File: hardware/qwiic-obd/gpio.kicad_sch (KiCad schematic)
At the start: 25 parts, among them J401 1x4, SW401 SW_Push, SW402 SW_Push, U401 TCA9534, U402 MCP3423, U403 TCA9534, U404 APX823-31W5G-7

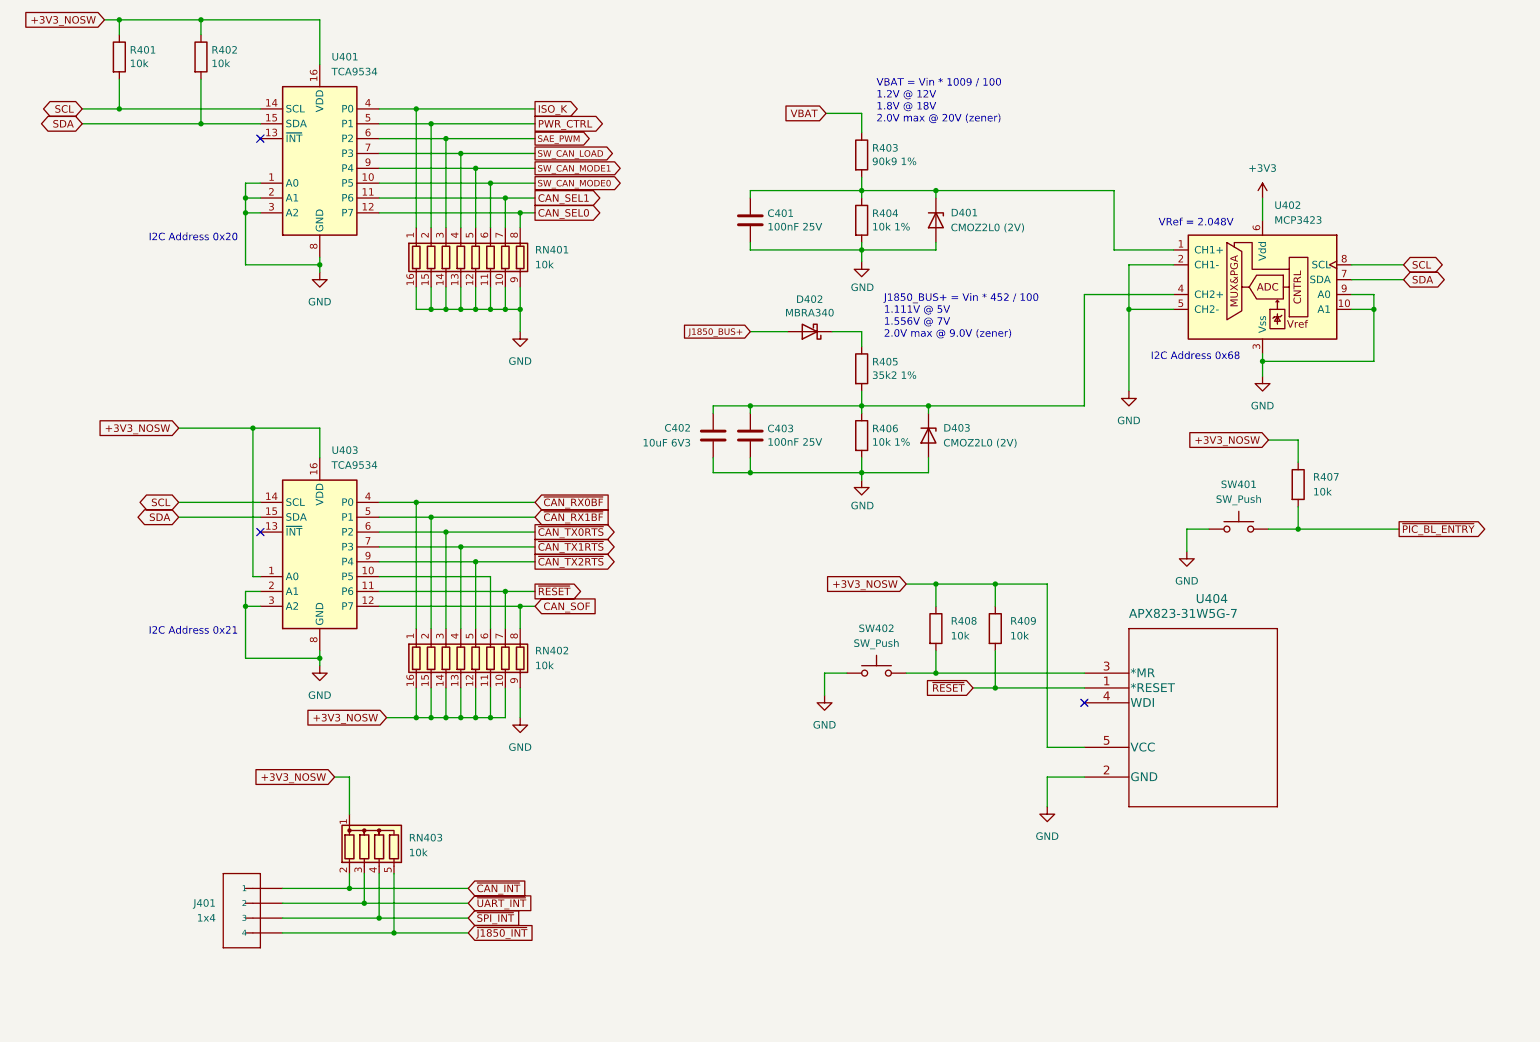
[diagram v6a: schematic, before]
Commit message: Switch out the PIC for an ATtiny424.
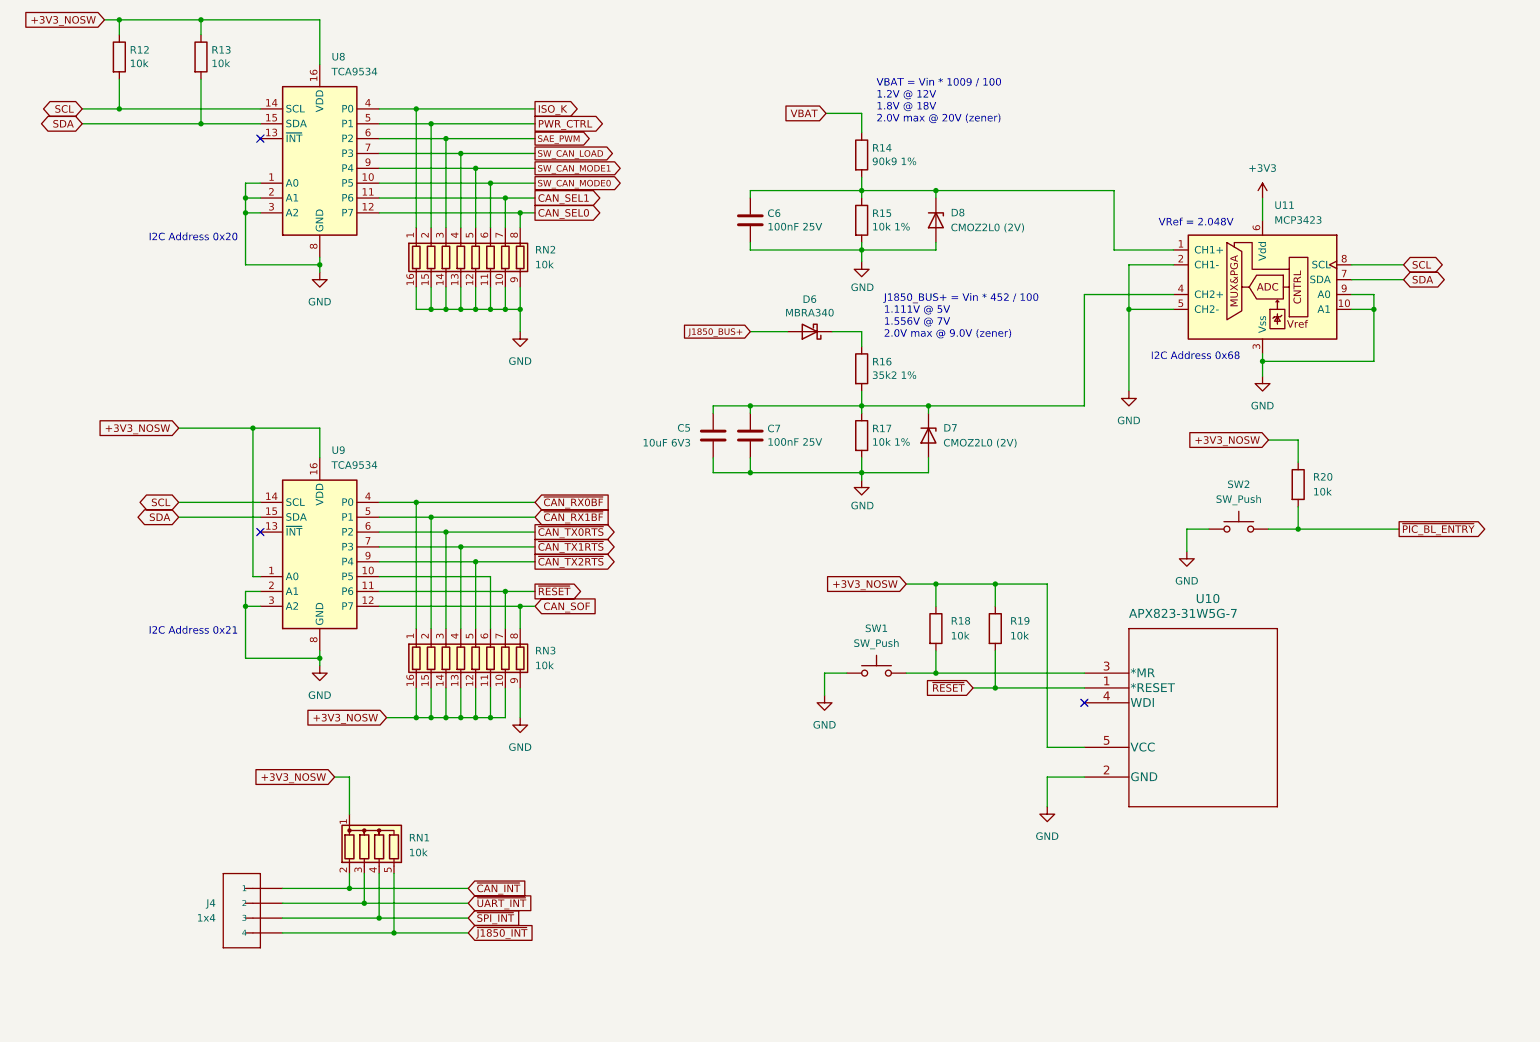
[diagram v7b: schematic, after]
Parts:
- renumbered C402 to C5, C401 to C6, C403 to C7, D402 to D6, D403 to D7, D401 to D8, J401 to J4, R401 to R12, R402 to R13, R403 to R14, R404 to R15, R405 to R16, R406 to R17, R408 to R18, R409 to R19, R407 to R20, RN403 to RN1, RN401 to RN2, RN402 to RN3, SW402 to SW1, SW401 to SW2, U404 to U10, U402 to U11, U401 to U8, U403 to U9
